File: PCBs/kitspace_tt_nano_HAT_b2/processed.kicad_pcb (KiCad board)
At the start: 2 copper layers, 34 x 59 mm, 25 parts, among them J1 Conn_01x04_Male, J10 Conn_01x06_Male, J11 Conn_01x02_Male, J12 Conn_01x06_Male, J2 Conn_01x06_Male, J3 Conn_01x04_Female, J4 Conn_01x03_Male, J5 Conn_01x03_Male, J6 Conn_01x03_Male, J7 Conn_01x03_Male, J8 Conn_01x03_Male, J9 Conn_01x03_Male

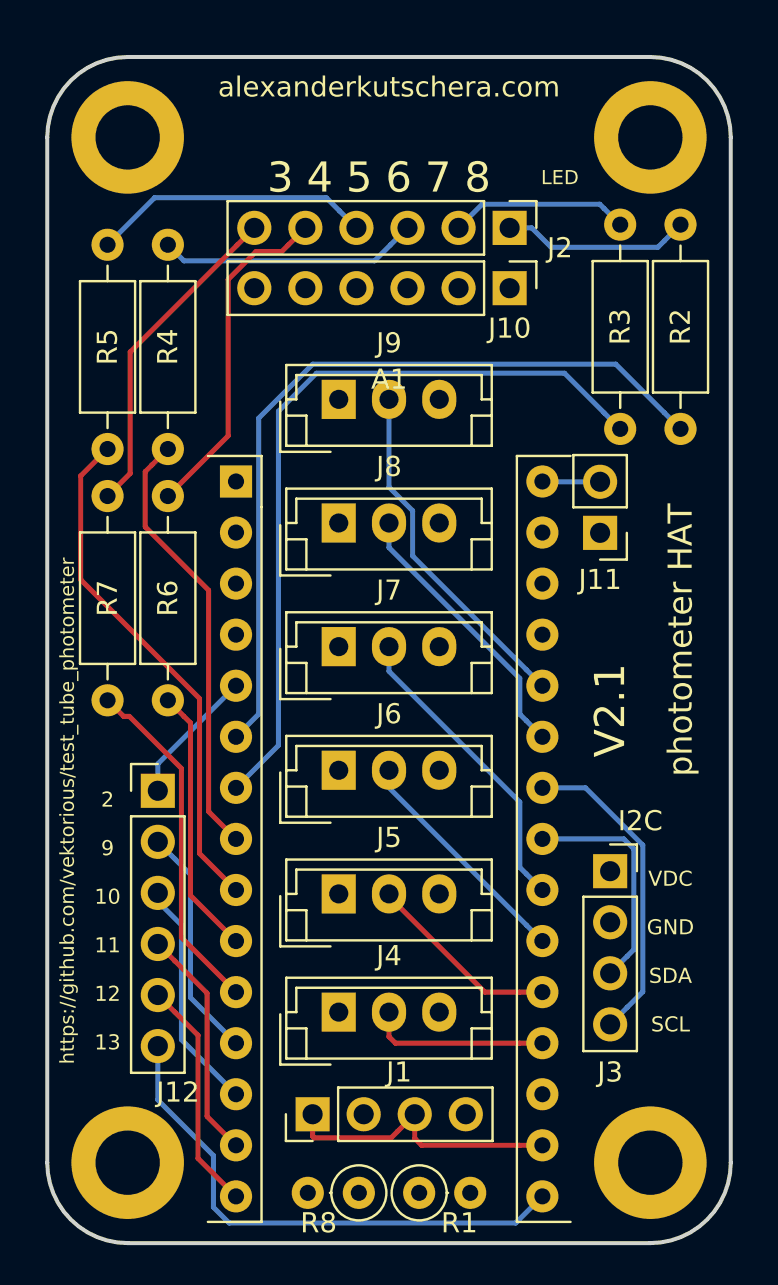
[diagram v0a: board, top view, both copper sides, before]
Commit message: recheck all circuits and clean up fill zone by rerouting the nets using freerouting and manually
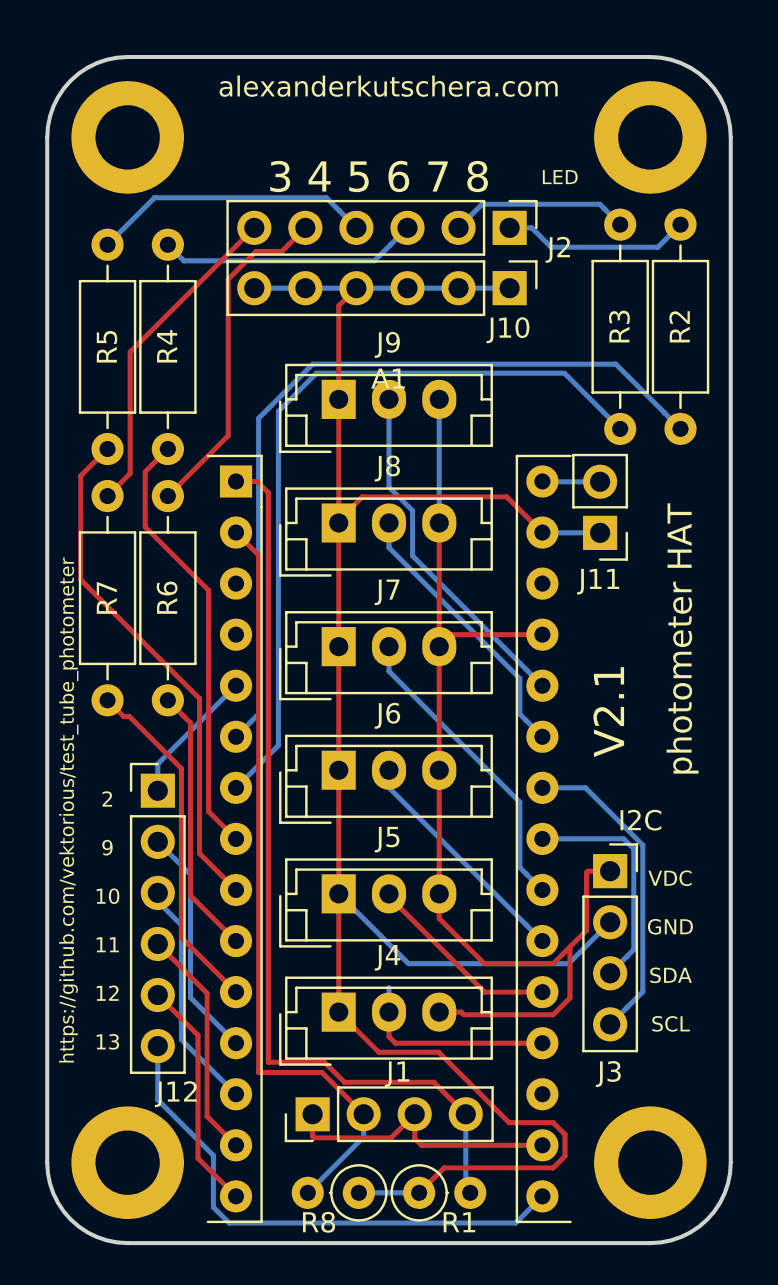
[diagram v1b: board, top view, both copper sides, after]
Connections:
- A1 pad 1: (no net) -> Net-(A1-Pad1)
- A1 pad 2: (no net) -> Net-(A1-Pad2)
- A1 pad 27: (no net) -> Net-(A1-Pad27)
- A1 pad 29: (no net) -> GND
- J1 pad 2: (no net) -> Net-(A1-Pad2)
- J1 pad 4: (no net) -> Net-(A1-Pad1)
- J10 pad 1: (no net) -> GND
- J10 pad 2: (no net) -> GND
- J10 pad 3: (no net) -> GND
- J10 pad 4: (no net) -> GND
- J10 pad 5: (no net) -> GND
- J10 pad 6: (no net) -> GND
- J11 pad 1: (no net) -> GND
- J3 pad 1: (no net) -> Net-(A1-Pad27)
- J3 pad 2: (no net) -> GND
- J4 pad 1: (no net) -> GND
- J4 pad 3: (no net) -> Net-(A1-Pad27)
- J5 pad 1: (no net) -> GND
- J5 pad 3: (no net) -> Net-(A1-Pad27)
- J6 pad 1: (no net) -> GND
- J6 pad 3: (no net) -> Net-(A1-Pad27)
- J7 pad 1: (no net) -> GND
- J7 pad 3: (no net) -> Net-(A1-Pad27)
- J8 pad 1: (no net) -> GND
- J8 pad 3: (no net) -> Net-(A1-Pad27)
- J9 pad 1: (no net) -> GND
- J9 pad 3: (no net) -> Net-(A1-Pad27)
- R1 pad 1: (no net) -> GND
- R1 pad 2: (no net) -> Net-(A1-Pad1)
- R8 pad 1: (no net) -> GND
- R8 pad 2: (no net) -> Net-(A1-Pad2)
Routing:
- net GND: track 0.00 -> 105.1 mm
- net Net-(A1-Pad27): track 0.00 -> 53.7 mm
- net Net-(A1-Pad1): track 0.00 -> 45.1 mm
- net Net-(A1-Pad2): track 0.00 -> 38.5 mm
- net Net-(A1-Pad19): track 8.99 -> 10.5 mm
- net Net-(A1-Pad22): track 15.3 -> 16.2 mm

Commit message: clean psbc that are missed before
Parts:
- gave numbers to parts that had none: 4
